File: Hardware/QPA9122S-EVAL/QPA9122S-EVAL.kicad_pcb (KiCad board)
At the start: 2 copper layers, 58.5 x 32.9 mm, 22 parts, among them IC1 QPA9122TR7, J1 Conn_Coaxial, J2 Conn_Coaxial, J3 Conn_01x02_Pin, J4 Conn_01x02_Pin, J5 Conn_01x02_Pin, J6 Conn_Coaxial, J7 Conn_Coaxial

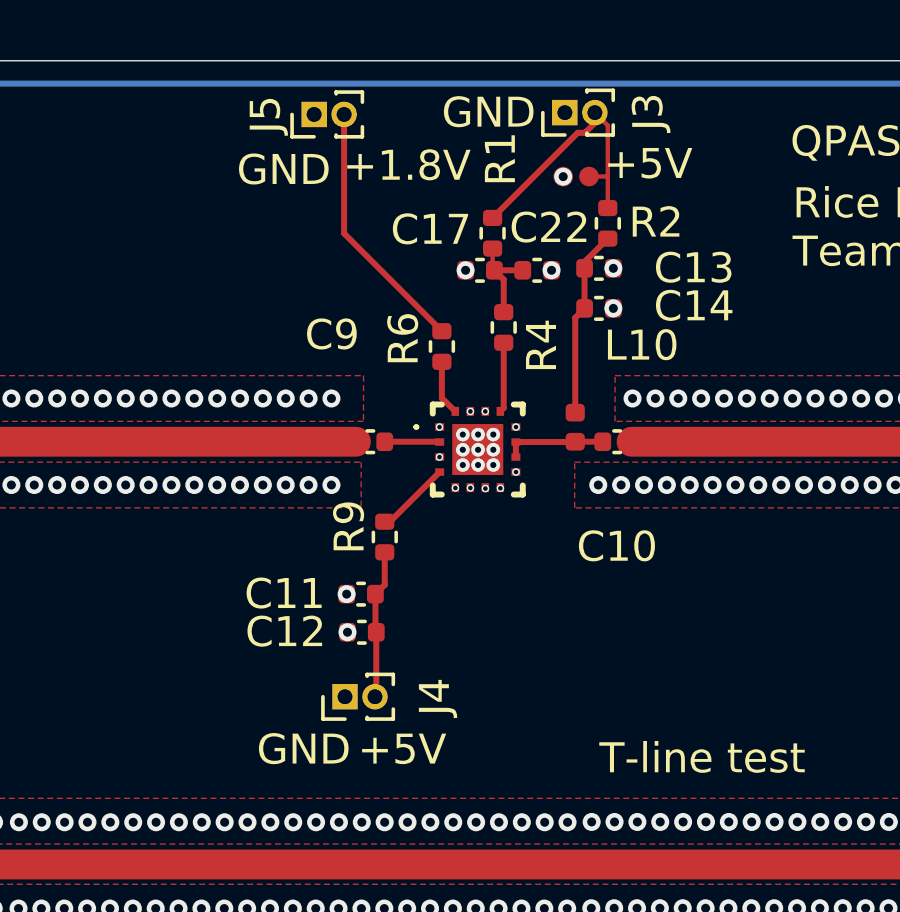
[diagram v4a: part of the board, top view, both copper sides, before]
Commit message: DRC and header re-sizing
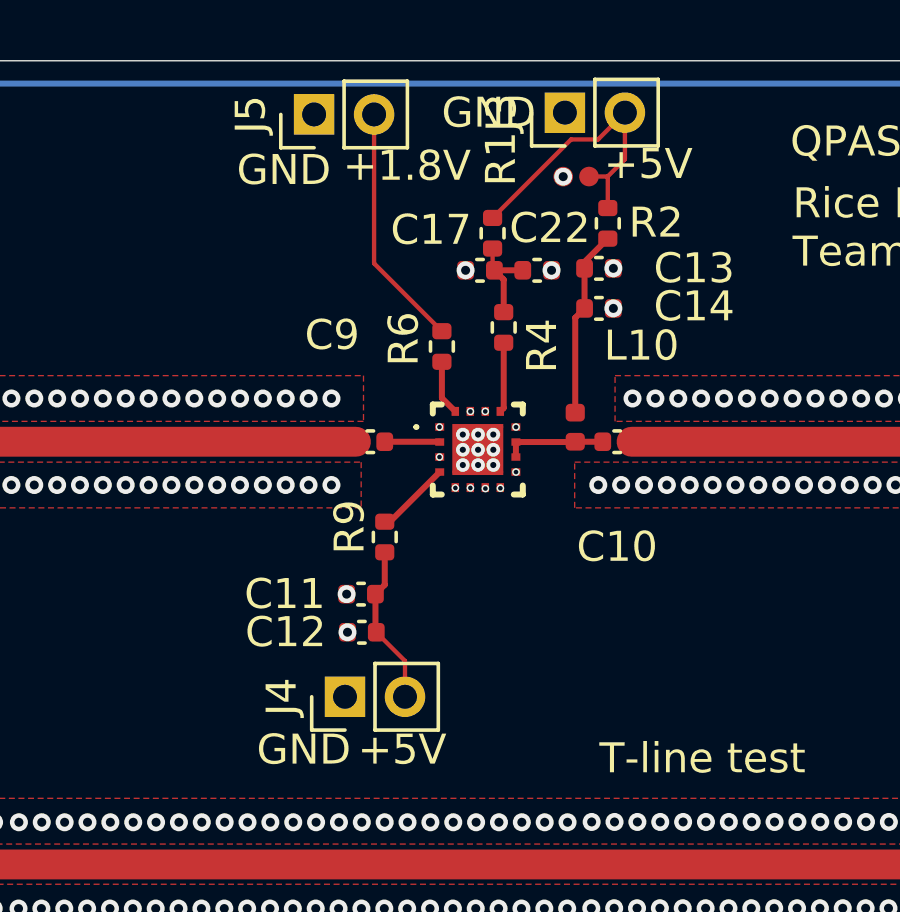
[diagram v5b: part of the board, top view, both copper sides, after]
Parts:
- J3, J4, J5: footprint Connector_PinHeader_1.00mm:PinHeader_1x02_P1.00mm_Vertical -> Connector_PinHeader_2.00mm:PinHeader_1x02_P2.00mm_Vertical
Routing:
- net VCC: track 9.02 -> 9.88 mm

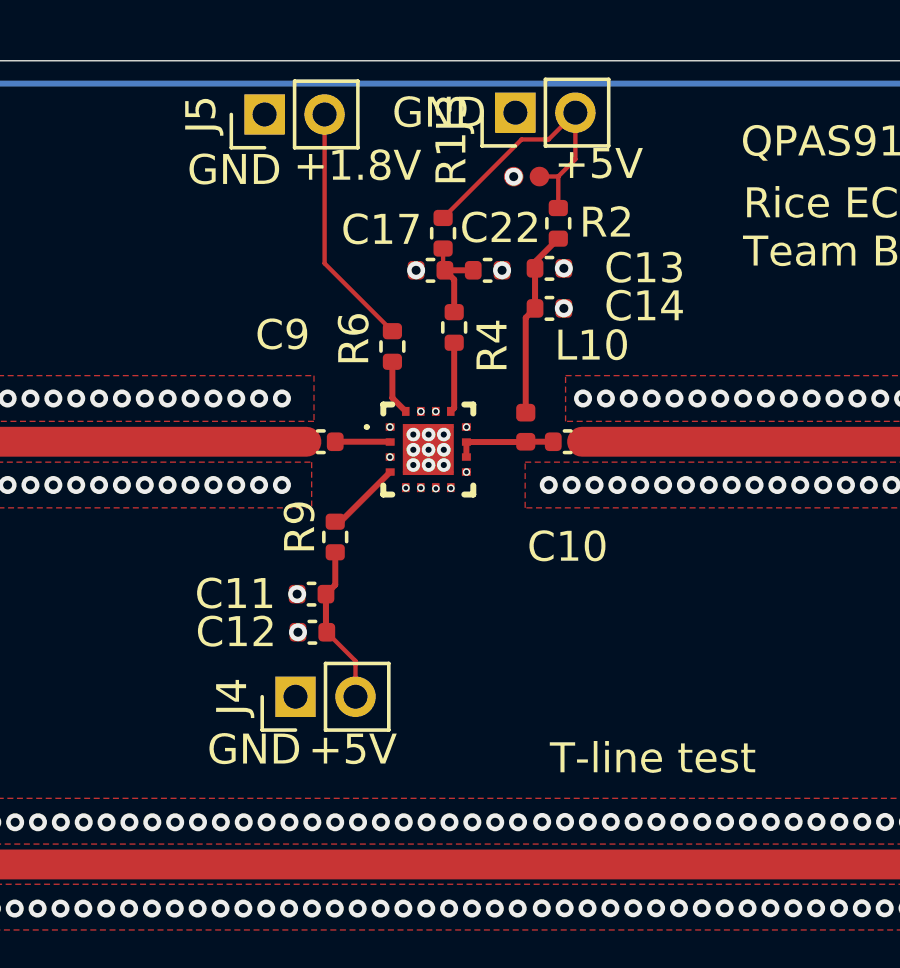
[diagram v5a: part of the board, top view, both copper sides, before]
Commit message: DRC and connector sizing
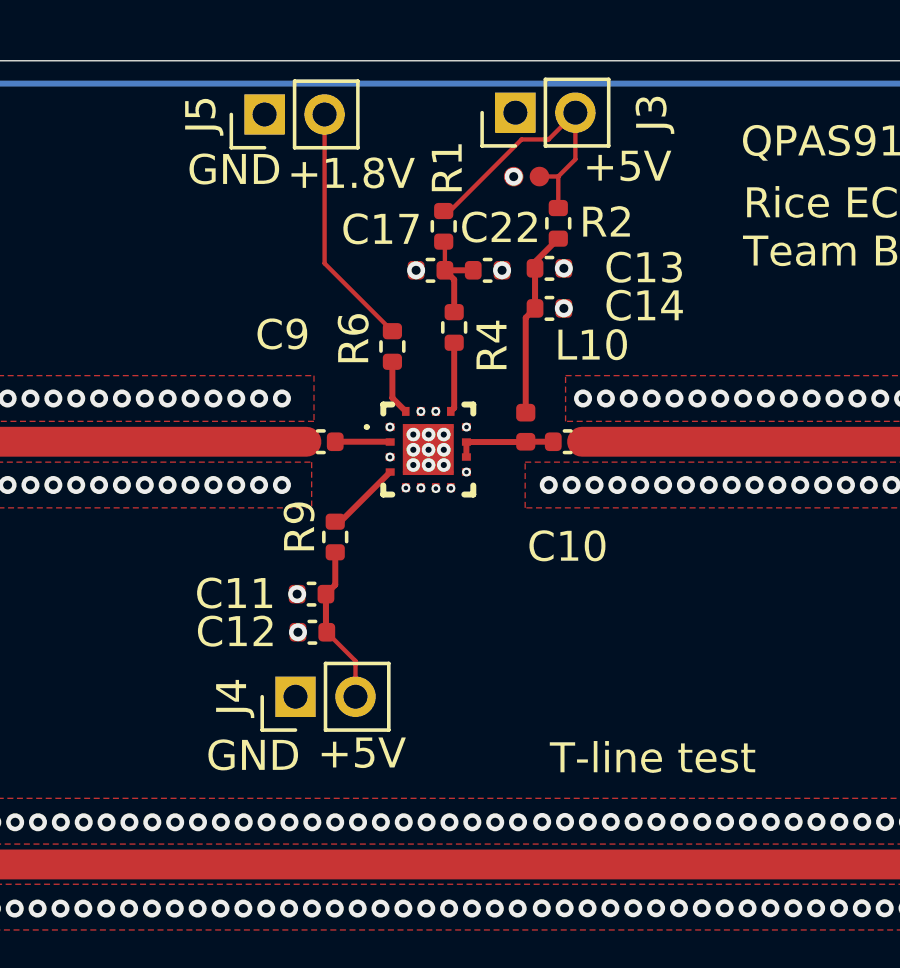
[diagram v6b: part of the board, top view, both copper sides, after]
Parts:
- moved R1 0.23 mm to (119.8, 86.8)
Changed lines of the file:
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@@
 			(at 0 4.11 90)
 			(layer "F.Fab")
+			(hide yes)
 			(effects
 				(font
@@
 		(tags "Through hole pin header THT 1x02 2.00mm single row")
 		(property "Reference" "J3"
-			(at 0 -2.11 90)
+			(at 0 4.56 90)
 			(layer "F.SilkS")
 			(effects
@@
 			(at 0 4.11 90)
 			(layer "F.Fab")
+			(hide yes)
 			(effects
 				(font
@@
 	(footprint "Resistor_SMD:R_0402_1005Metric"
 		(layer "F.Cu")
-		(at 119.8 87.03 90)
+		(at 119.82 86.8 90)
 		(descr "Resistor SMD 0402 (1005 Metric), square (rectangular) end terminal, IPC-7351 nominal, (Body size source: IPC-SM-782 page 72, https://www.pcb-3d.com/wordpress/wp-content/uploads/ipc-sm-782a_amendment_1_and_2.pdf), generated with kicad-footprint-generator")
 		(tags "resistor")
 		(property "Reference" "R1"
-			(at 2.48 0.28 90)
+			(at 1.95 0.14 90)
 			(layer "F.SilkS")
 			(effects
@@
 	)
 	(gr_text "GND\n"
-		(at 111.935 104.83 0)
+		(at 111.9 105.04 0)
 		(layer "F.SilkS")
 		(effects
@@
 		)
 	)
-	(gr_text "GND\n"
-		(at 118.1 83.6 0)
-		(layer "F.SilkS")
-		(effects
-			(font
-				(size 1 1)
-				(thickness 0.1)
-			)
-			(justify left bottom)
-		)
-	)
 	(gr_text "QPAS9122 Eval Board"
 		(at 129.72 84.56 0)
@@
 	)
 	(gr_text "+5V"
-		(at 123.51 85.31 0)
+		(at 124.46 85.4 0)
 		(layer "F.SilkS")
 		(effects
@@
 	)
 	(gr_text "+1.8V"
-		(at 114.81 85.37 0)
+		(at 114.6 85.64 0)
 		(layer "F.SilkS")
 		(effects
@@
 	)
 	(gr_text "+5V"
-		(at 115.305 104.83 0)
+		(at 115.61 104.96 0)
 		(layer "F.SilkS")
 		(effects
@@
 	(via
 		(at 119.56 95.54)
-		(size 0.254)
-		(drill 0.1524)
+		(size 0.3)
+		(drill 0.15)
 		(layers "F.Cu" "B.Cu")
 		(free yes)
@@
 	(via
 		(at 119.06 92.97)
-		(size 0.254)
-		(drill 0.1524)
+		(size 0.3)
+		(drill 0.15)
 		(layers "F.Cu" "B.Cu")
 		(free yes)
@@
 	(via
 		(at 118.56 95.52)
-		(size 0.254)
-		(drill 0.1524)
+		(size 0.3)
+		(drill 0.15)
 		(layers "F.Cu" "B.Cu")
 		(free yes)
@@
 	(via
 		(at 118.03 94.49)
-		(size 0.254)
-		(drill 0.1524)
+		(size 0.3)
+		(drill 0.15)
 		(layers "F.Cu" "B.Cu")
 		(free yes)
@@
 	(via
 		(at 120.58 94.99)
-		(size 0.254)
-		(drill 0.1524)
+		(size 0.3)
+		(drill 0.15)
 		(layers "F.Cu" "B.Cu")
 		(free yes)
@@
 	(via
 		(at 120.58 93.49)
-		(size 0.254)
-		(drill 0.1524)
+		(size 0.3)
+		(drill 0.15)
 		(layers "F.Cu" "B.Cu")
 		(free yes)
@@
 	(via
 		(at 119.5567 92.969)
-		(size 0.254)
-		(drill 0.1524)
+		(size 0.3)
+		(drill 0.15)
 		(layers "F.Cu" "B.Cu")
 		(free yes)
@@
 	(via
 		(at 119.06 95.52)
-		(size 0.254)
-		(drill 0.1524)
+		(size 0.3)
+		(drill 0.15)
 		(layers "F.Cu" "B.Cu")
 		(free yes)
@@
 	(via
 		(at 118.03 93.49)
-		(size 0.254)
-		(drill 0.1524)
+		(size 0.3)
+		(drill 0.15)
 		(layers "F.Cu" "B.Cu")
 		(free yes)
@@
 	(via
 		(at 120.06 95.53)
-		(size 0.254)
-		(drill 0.1524)
+		(size 0.3)
+		(drill 0.15)
 		(layers "F.Cu" "B.Cu")
 		(free yes)
@@
 	)
 	(segment
+		(start 120.03 86.29)
+		(end 122.41683 83.90317)
+		(width 0.14478)
+		(layer "F.Cu")
+		(net 7)
+	)
+	(segment
+		(start 119.82 86.29)
+		(end 120.03 86.29)
+		(width 0.14478)
+		(layer "F.Cu")
+		(net 7)
+	)
+	(segment
 		(start 123.637805 85.137805)
 		(end 123.64 85.14)
@@
 	)
 	(segment
-		(start 119.8 86.52)
-		(end 122.41683 83.90317)
-		(width 0.14478)
-		(layer "F.Cu")
-		(net 7)
-	)
-	(segment
 		(start 123.31683 83.90317)
 		(end 124.21 83.01)
@@
 	)
 	(segment
-		(start 119.8 87.54)
-		(end 119.8 88.205)
+		(start 119.86 87.35)
+		(end 119.82 87.31)
 		(width 0.14478)
 		(layer "F.Cu")
@@
 		(layer "F.Cu")
 		(net 14)
+	)
+	(segment
+		(start 119.86 88.265)
+		(end 119.86 87.35)
+		(width 0.14478)
+		(layer "F.Cu")
+		(net 14)

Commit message: Fixed JLCPCB Errors
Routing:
- net GND: track 1.42 -> 9.73 mm, vias 280 -> 270
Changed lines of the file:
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@@
 			(drillshape 0)
 			(scaleselection 1)
-			(outputdirectory "")
+			(outputdirectory "QPAS122S-EVAL-GRB/")
 		)
 	)
@@
 	)
 	(segment
+		(start 118.5567 93.489)
+		(end 118.80745 93.73975)
+		(width 0.14478)
+		(layer "F.Cu")
+		(net 5)
+	)
+	(segment
+		(start 119.5567 95.509)
+		(end 119.5567 95.0225)
+		(width 0.14478)
+		(layer "F.Cu")
+		(net 5)
+	)
+	(segment
+		(start 119.5567 93.473)
+		(end 119.82345 93.73975)
+		(width 0.14478)
+		(layer "F.Cu")
+		(net 5)
+	)
+	(segment
+		(start 118.0367 94.489)
+		(end 118.5662 94.489)
+		(width 0.14478)
+		(layer "F.Cu")
+		(net 5)
+	)
+	(segment
+		(start 119.5567 92.969)
+		(end 119.5567 93.473)
+		(width 0.14478)
+		(layer "F.Cu")
+		(net 5)
+	)
+	(segment
 		(start 119.31545 94.24775)
 		(end 119.3067 94.239)
@@
 	)
 	(segment
+		(start 119.0567 93.4905)
+		(end 118.80745 93.73975)
+		(width 0.14478)
+		(layer "F.Cu")
+		(net 5)
+	)
+	(segment
 		(start 120.0567 93.489)
 		(end 119.79035 93.75535)
@@
 	)
 	(segment
+		(start 120.5767 93.489)
+		(end 120.0742 93.489)
+		(width 0.14478)
+		(layer "F.Cu")
+		(net 5)
+	)
+	(segment
+		(start 119.5567 95.0225)
+		(end 119.82345 94.75575)
+		(width 0.14478)
+		(layer "F.Cu")
+		(net 5)
+	)
+	(segment
+		(start 118.5567 95.509)
+		(end 118.5567 95.0065)
+		(width 0.14478)
+		(layer "F.Cu")
+		(net 5)
+	)
+	(segment
+		(start 120.5767 94.989)
+		(end 120.0567 94.989)
+		(width 0.14478)
+		(layer "F.Cu")
+		(net 5)
+	)
+	(segment
 		(start 118.5567 94.989)
 		(end 118.77435 94.77135)
@@
 	(segment
 		(start 120.0567 94.989)
+		(end 119.82345 94.75575)
+		(width 0.14478)
+		(layer "F.Cu")
+		(net 5)
+	)
+	(segment
+		(start 119.0567 95.0145)
+		(end 119.31545 94.75575)
+		(width 0.14478)
+		(layer "F.Cu")
+		(net 5)
+	)
+	(segment
+		(start 118.5567 95.0065)
+		(end 118.80745 94.75575)
+		(width 0.14478)
+		(layer "F.Cu")
+		(net 5)
+	)
+	(segment
+		(start 120.0567 94.989)
 		(end 119.78535 94.71765)
 		(width 0.2)
@@
 	)
 	(segment
+		(start 119.0567 95.509)
+		(end 119.0567 95.0145)
+		(width 0.14478)
+		(layer "F.Cu")
+		(net 5)
+	)
+	(segment
+		(start 118.5662 94.489)
+		(end 118.80745 94.24775)
+		(width 0.14478)
+		(layer "F.Cu")
+		(net 5)
+	)
+	(segment
+		(start 120.0567 95.509)
+		(end 120.0567 94.989)
+		(width 0.14478)
+		(layer "F.Cu")
+		(net 5)
+	)
+	(segment
+		(start 118.0367 93.489)
+		(end 118.5567 93.489)
+		(width 0.14478)
+		(layer "F.Cu")
+		(net 5)
+	)
+	(segment
+		(start 120.0742 93.489)
+		(end 119.82345 93.73975)
+		(width 0.14478)
+		(layer "F.Cu")
+		(net 5)
+	)
+	(segment
+		(start 119.0567 92.969)
+		(end 119.0567 93.4905)
+		(width 0.14478)
+		(layer "F.Cu")
+		(net 5)
+	)
+	(segment
 		(start 119.5567 94.489)
 		(end 119.31545 94.24775)
@@
 	)
 	(via
-		(at 119.56 95.54)
-		(size 0.3)
-		(drill 0.15)
-		(layers "F.Cu" "B.Cu")
-		(free yes)
-		(net 5)
-	)
-	(via
 		(at 134.370975 92.538)
 		(size 0.6)
@@
 	)
 	(via
-		(at 119.06 92.97)
-		(size 0.3)
-		(drill 0.15)
-		(layers "F.Cu" "B.Cu")
-		(free yes)
-		(net 5)
-	)
-	(via
 		(at 105.53433 106.664)
 		(size 0.6)
@@
 	)
 	(via
-		(at 118.56 95.52)
-		(size 0.3)
-		(drill 0.15)
-		(layers "F.Cu" "B.Cu")
-		(free yes)
-		(net 5)
-	)
-	(via
 		(at 119.82345 93.73975)
 		(size 0.4572)
@@
 	)
 	(via
-		(at 118.03 94.49)
-		(size 0.3)
-		(drill 0.15)
-		(layers "F.Cu" "B.Cu")
-		(free yes)
-		(net 5)
-	)
-	(via
 		(at 113.142 109.54)
 		(size 0.6)
@@
 	)
 	(via
-		(at 120.58 94.99)
-		(size 0.3)
-		(drill 0.15)
-		(layers "F.Cu" "B.Cu")
-		(free yes)
-		(net 5)
-	)
-	(via
 		(at 131.322975 92.538)
 		(size 0.6)
@@
 	)
 	(via
-		(at 120.58 93.49)
-		(size 0.3)
-		(drill 0.15)
-		(layers "F.Cu" "B.Cu")
-		(free yes)
-		(net 5)
-	)
-	(via
 		(at 130.942872 95.422)
 		(size 0.6)
@@
 	)
 	(via
-		(at 119.5567 92.969)
-		(size 0.3)
-		(drill 0.15)
-		(layers "F.Cu" "B.Cu")
-		(free yes)
-		(net 5)
-	)
-	(via
 		(at 124.846872 95.422)
 		(size 0.6)
@@
 	)
 	(via
-		(at 119.06 95.52)
-		(size 0.3)
-		(drill 0.15)
-		(layers "F.Cu" "B.Cu")
-		(free yes)
-		(net 5)
-	)
-	(via
 		(at 139.854 109.53)
 		(size 0.6)
@@
 	)
 	(via
-		(at 118.03 93.49)
-		(size 0.3)
-		(drill 0.15)
-		(layers "F.Cu" "B.Cu")
-		(free yes)
-		(net 5)
-	)
-	(via
 		(at 134.52 109.53)
 		(size 0.6)
@@
 		(layers "F.Cu" "B.Cu")
 		(free yes)
-		(net 5)
-	)
-	(via
-		(at 120.06 95.53)
-		(size 0.3)
-		(drill 0.15)
-		(layers "F.Cu" "B.Cu")
-		(free yes)
